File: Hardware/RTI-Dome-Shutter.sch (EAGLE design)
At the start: 42 parts, among them IC1 24AA128ST, IC5 74LVC245, IC6 74ABT245

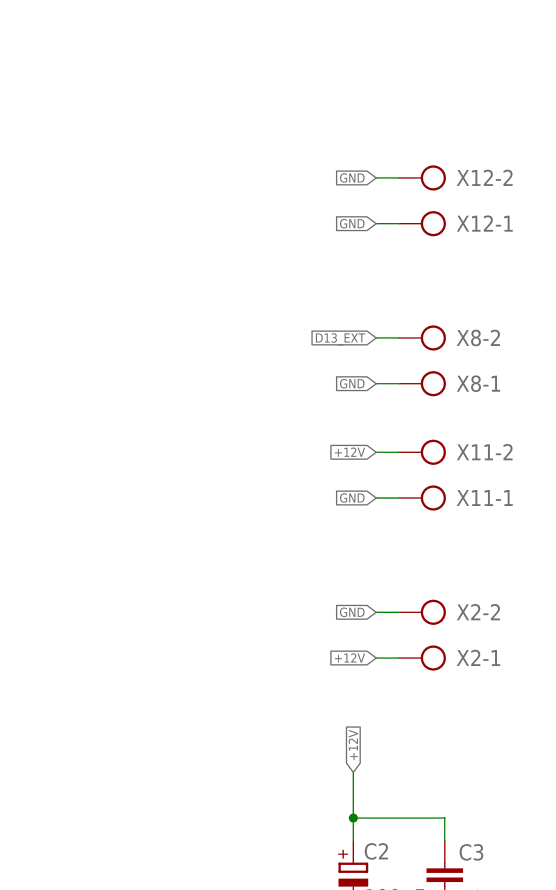
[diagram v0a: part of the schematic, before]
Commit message: Added powerpole to shutter shield
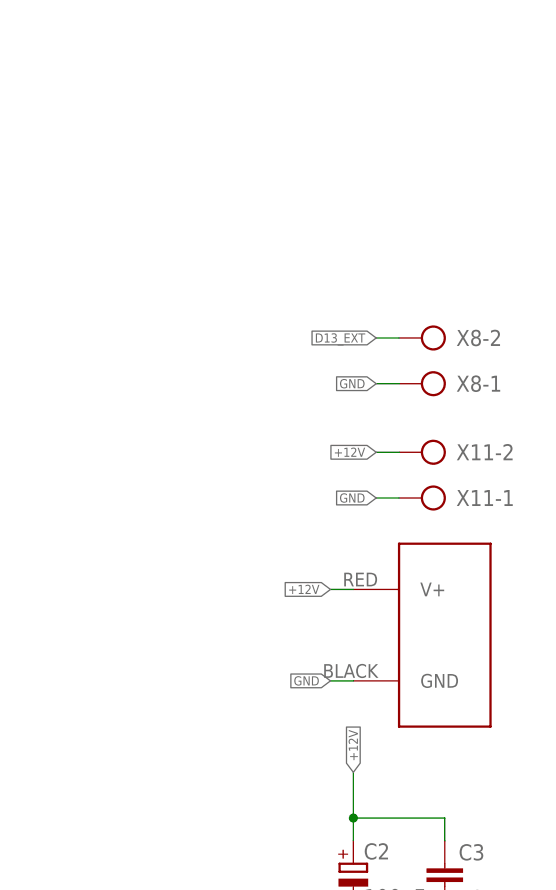
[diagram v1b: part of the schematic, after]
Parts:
- removed X12, X2: (no value), con-ptr500:AK500/2
- added J1: POWERPOLE_POWER45A, powerpoles:POWERPOLE_POWER45A
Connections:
- net +12V: now also J1.V+; no longer X2-1.KL
- net GND: now also J1.GND; no longer X12-1.KL, X12-2.KL, X2-2.KL
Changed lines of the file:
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@@
 </classes>
 <parts>
-<part name="X2" library="con-ptr500" deviceset="AK500/2" device=""/>
 <part name="X4" library="con-ptr500" deviceset="AK500/3" device=""/>
 <part name="X1" library="con-ptr500" deviceset="AK500/2" device=""/>
@@
 <part name="R3" library="rti" deviceset="R-EU" device="'0805'" value="1K"/>
 <part name="C5" library="rti" deviceset="C-EU" device="'0805'" value="100nF"/>
-<part name="X12" library="con-ptr500" deviceset="AK500/2" device=""/>
 <part name="GND12" library="supply1" deviceset="GND" device=""/>
 <part name="P+1" library="supply1" deviceset="VCC" device=""/>
@@
 <part name="GND7" library="supply1" deviceset="GND" device=""/>
 <part name="R22" library="rti" deviceset="R-EU" device="'0805'" value="4.7K"/>
+<part name="J1" library="powerpoles" deviceset="POWERPOLE_POWER" device="45A"/>
 </parts>
 <sheets>
@@
 </plain>
 <instances>
-<instance part="X2" gate="-1" x="378.46" y="81.28" rot="R180"/>
-<instance part="X2" gate="-2" x="378.46" y="86.36" rot="R180"/>
 <instance part="X4" gate="-1" x="378.46" y="218.44" rot="R180"/>
 <instance part="X4" gate="-2" x="378.46" y="223.52" rot="R180"/>
@@
 <instance part="R3" gate="G$1" x="40.64" y="248.92" rot="R90"/>
 <instance part="C5" gate="G$1" x="114.3" y="180.34"/>
-<instance part="X12" gate="-1" x="378.46" y="129.54" rot="R180"/>
-<instance part="X12" gate="-2" x="378.46" y="134.62" rot="R180"/>
 <instance part="GND12" gate="1" x="205.74" y="165.1"/>
 <instance part="P+1" gate="VCC" x="205.74" y="195.58"/>
@@
 <instance part="GND7" gate="1" x="187.96" y="226.06"/>
 <instance part="R22" gate="G$1" x="147.32" y="180.34" rot="R270"/>
+<instance part="J1" gate="G$1" x="378.46" y="83.82"/>
 </instances>
 <busses>
@@
 </segment>
 <segment>
-<pinref part="X2" gate="-2" pin="KL"/>
-<wire x1="370.84" y1="86.36" x2="373.38" y2="86.36" width="0.1524" layer="91"/>
-<label x="370.84" y="86.36" size="1.016" layer="95" rot="R180" xref="yes"/>
+<wire x1="365.76" y1="78.74" x2="368.3" y2="78.74" width="0.1524" layer="91"/>
+<label x="365.76" y="78.74" size="1.016" layer="95" rot="R180" xref="yes"/>
+<pinref part="J1" gate="G$1" pin="GND"/>
 </segment>
 <segment>
@@
 </segment>
 <segment>
-<pinref part="X12" gate="-1" pin="KL"/>
-<wire x1="370.84" y1="129.54" x2="373.38" y2="129.54" width="0.1524" layer="91"/>
-<label x="370.84" y="129.54" size="1.016" layer="95" rot="R180" xref="yes"/>
-</segment>
-<segment>
 <wire x1="116.84" y1="243.84" x2="119.38" y2="243.84" width="0.1524" layer="91"/>
 <label x="116.84" y="243.84" size="0.8128" layer="95" rot="R180" xref="yes"/>
@@
 <label x="187.96" y="238.76" size="0.8128" layer="95" rot="R180" xref="yes"/>
 <pinref part="IC6" gate="G$1" pin="A7"/>
-</segment>
-<segment>
-<pinref part="X12" gate="-2" pin="KL"/>
-<wire x1="370.84" y1="134.62" x2="373.38" y2="134.62" width="0.1524" layer="91"/>
-<label x="370.84" y="134.62" size="1.016" layer="95" rot="R180" xref="yes"/>
 </segment>
 <segment>
@@
 </segment>
 <segment>
-<pinref part="X2" gate="-1" pin="KL"/>
-<wire x1="370.84" y1="81.28" x2="373.38" y2="81.28" width="0.1524" layer="91"/>
-<label x="370.84" y="81.28" size="1.016" layer="95" rot="R180" xref="yes"/>
-</segment>
-<segment>
+<wire x1="365.76" y1="88.9" x2="368.3" y2="88.9" width="0.1524" layer="91"/>
+<label x="365.76" y="88.9" size="1.016" layer="95" rot="R180" xref="yes"/>
+<pinref part="J1" gate="G$1" pin="V+"/>
+</segment>
+<segment>

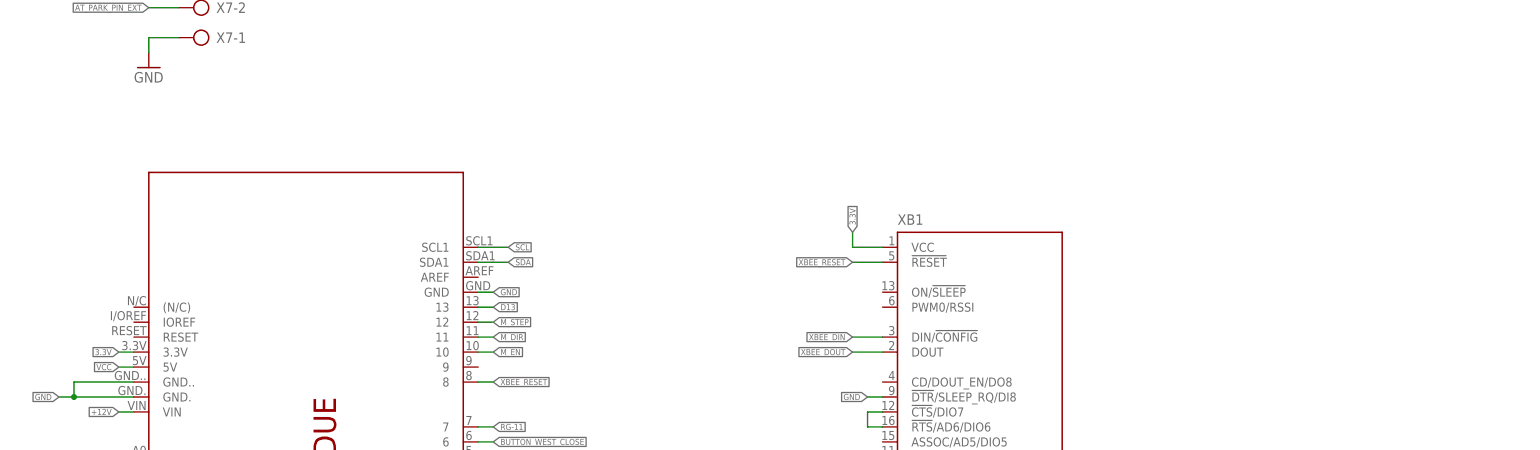
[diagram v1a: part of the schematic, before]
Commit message: Adding MCP120 for power on reset.
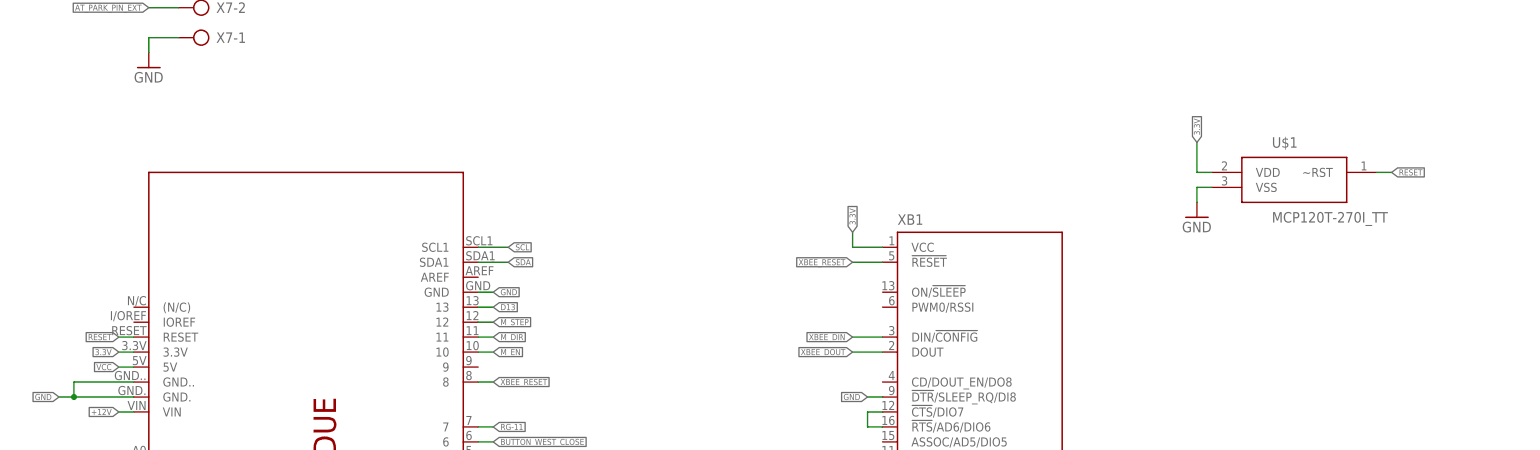
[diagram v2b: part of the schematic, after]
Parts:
- added U$1: MCP120T-270I_TT, MCP120T-270I_TT:MCP120T-270I_TT
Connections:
- new net RESET: PCB1.RESET, U$1.~RST
- net 3.3V: now also U$1.VDD
- net GND: now also U$1.VSS
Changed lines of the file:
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@@
 <part name="R22" library="rti" deviceset="R-EU" device="'0805'" value="4.7K"/>
 <part name="J1" library="powerpoles" deviceset="POWERPOLE_POWER" device="45A"/>
+<part name="U$1" library="MCP120T-270I_TT" deviceset="MCP120T-270I_TT" device=""/>
+<part name="GND9" library="supply1" deviceset="GND" device=""/>
 </parts>
 <sheets>
@@
 <instance part="R22" gate="G$1" x="147.32" y="180.34" rot="R270"/>
 <instance part="J1" gate="G$1" x="378.46" y="83.82"/>
+<instance part="U$1" gate="G$1" x="218.44" y="93.98"/>
+<instance part="GND9" gate="1" x="203.2" y="86.36"/>
 </instances>
 <busses>
@@
 <pinref part="GND7" gate="1" pin="GND"/>
 </segment>
+<segment>
+<pinref part="U$1" gate="G$1" pin="VSS"/>
+<wire x1="205.74" y1="91.44" x2="203.2" y2="91.44" width="0.1524" layer="91"/>
+<wire x1="203.2" y1="91.44" x2="203.2" y2="88.9" width="0.1524" layer="91"/>
+<pinref part="GND9" gate="1" pin="GND"/>
+</segment>
 </net>
 <net name="+12V" class="1">
@@
 <wire x1="116.84" y1="231.14" x2="119.38" y2="231.14" width="0.1524" layer="91"/>
 <label x="116.84" y="231.14" size="1.016" layer="95" rot="R180" xref="yes"/>
+</segment>
+<segment>
+<pinref part="U$1" gate="G$1" pin="VDD"/>
+<wire x1="205.74" y1="93.98" x2="203.2" y2="93.98" width="0.1524" layer="91"/>
+<wire x1="203.2" y1="93.98" x2="203.2" y2="99.06" width="0.1524" layer="91"/>
+<label x="203.2" y="99.06" size="1.016" layer="95" rot="R90" xref="yes"/>
 </segment>
 </net>
@@
 </segment>
 </net>
+<net name="RESET" class="0">
+<segment>
+<pinref part="PCB1" gate="G$1" pin="RESET"/>
+<wire x1="20.32" y1="66.04" x2="22.86" y2="66.04" width="0.1524" layer="91"/>
+<label x="20.32" y="66.04" size="1.016" layer="95" rot="R180" xref="yes"/>
+</segment>
+<segment>
+<pinref part="U$1" gate="G$1" pin="~RST"/>
+<wire x1="236.22" y1="93.98" x2="233.68" y2="93.98" width="0.1524" layer="91"/>
+<label x="236.22" y="93.98" size="1.016" layer="95" xref="yes"/>
+</segment>
+</net>

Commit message: Fix some componenent manufacturer reference
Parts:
- IC6: device rti:74LVC245 -> rti:74ABT245
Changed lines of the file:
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@@
 <part name="X6" library="con-ptr500" deviceset="AK500/6" device=""/>
 <part name="IC5" library="rti" deviceset="74*245" device="" technology="LVC"/>
-<part name="IC6" library="rti" deviceset="74*245" device="" technology="LVC" value="74ABT245"/>
+<part name="IC6" library="rti" deviceset="74*245" device="" technology="ABT" value="74ABT245"/>
 <part name="GND7" library="supply1" deviceset="GND" device=""/>
 <part name="R22" library="rti" deviceset="R-EU" device="'0805'" value="4.7K"/>

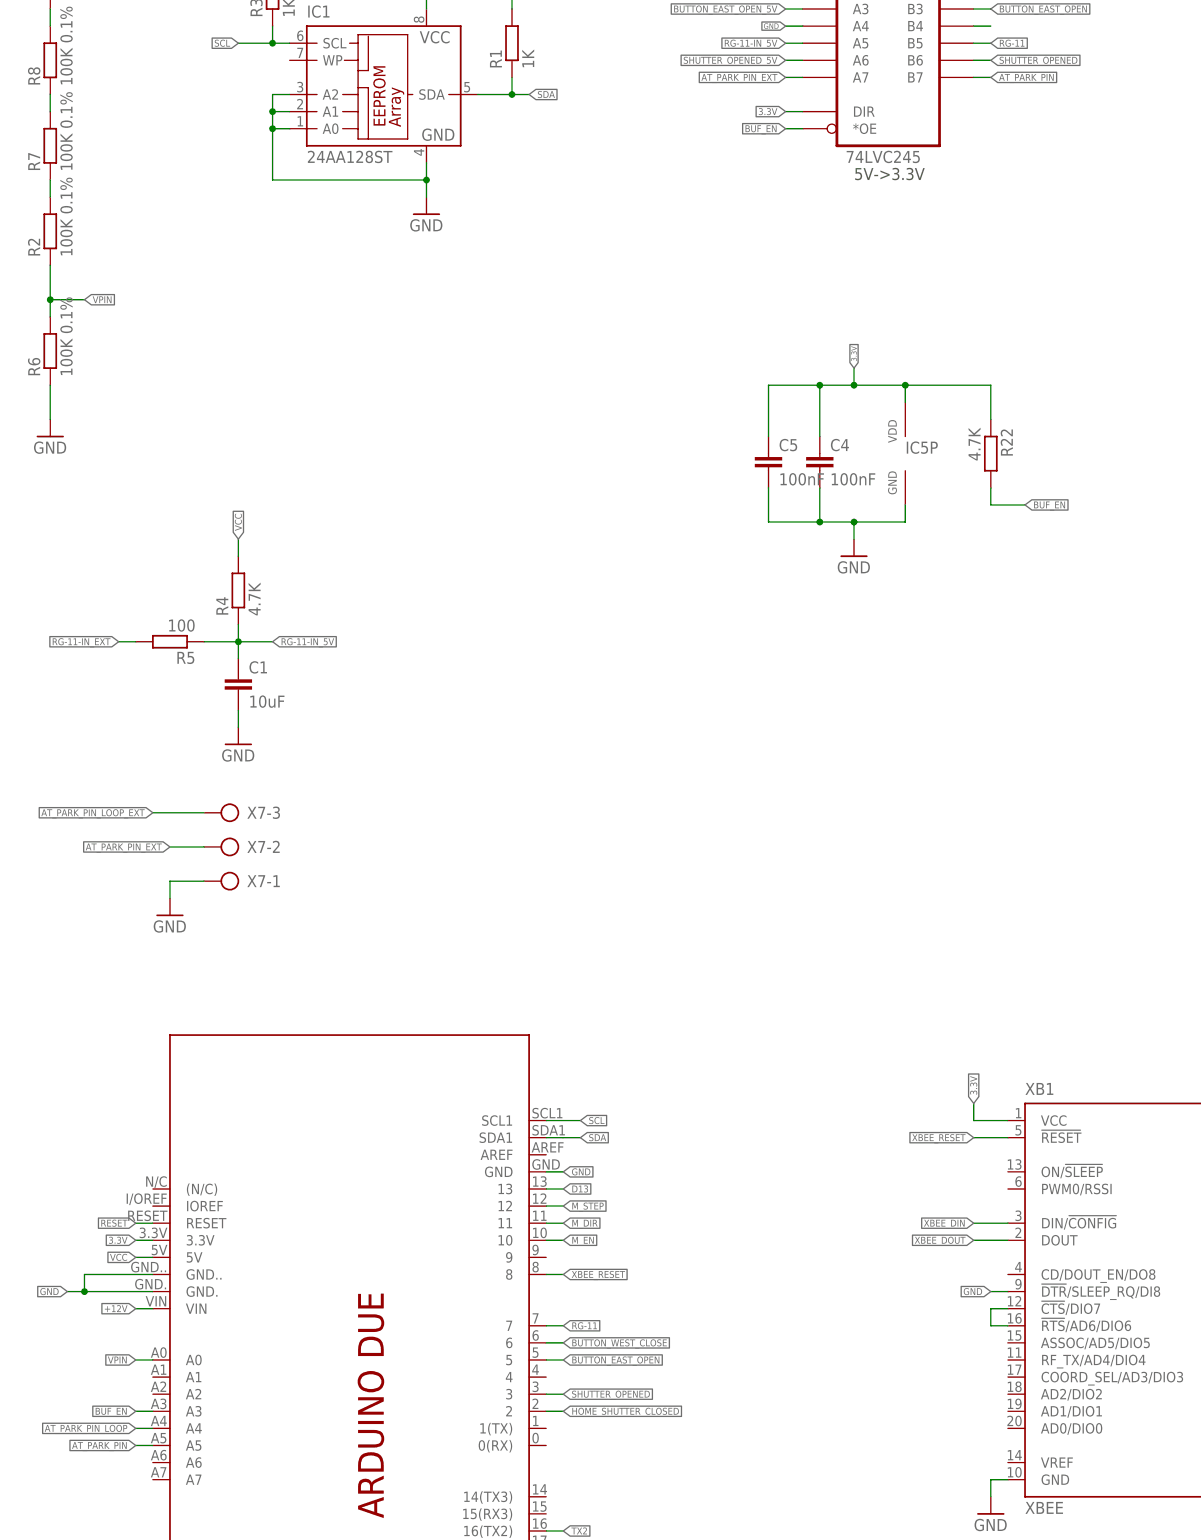
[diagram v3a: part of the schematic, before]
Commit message: Added FTDI reset as it wasn't doing a proper reset on power up. Finished IP config in the plugin.
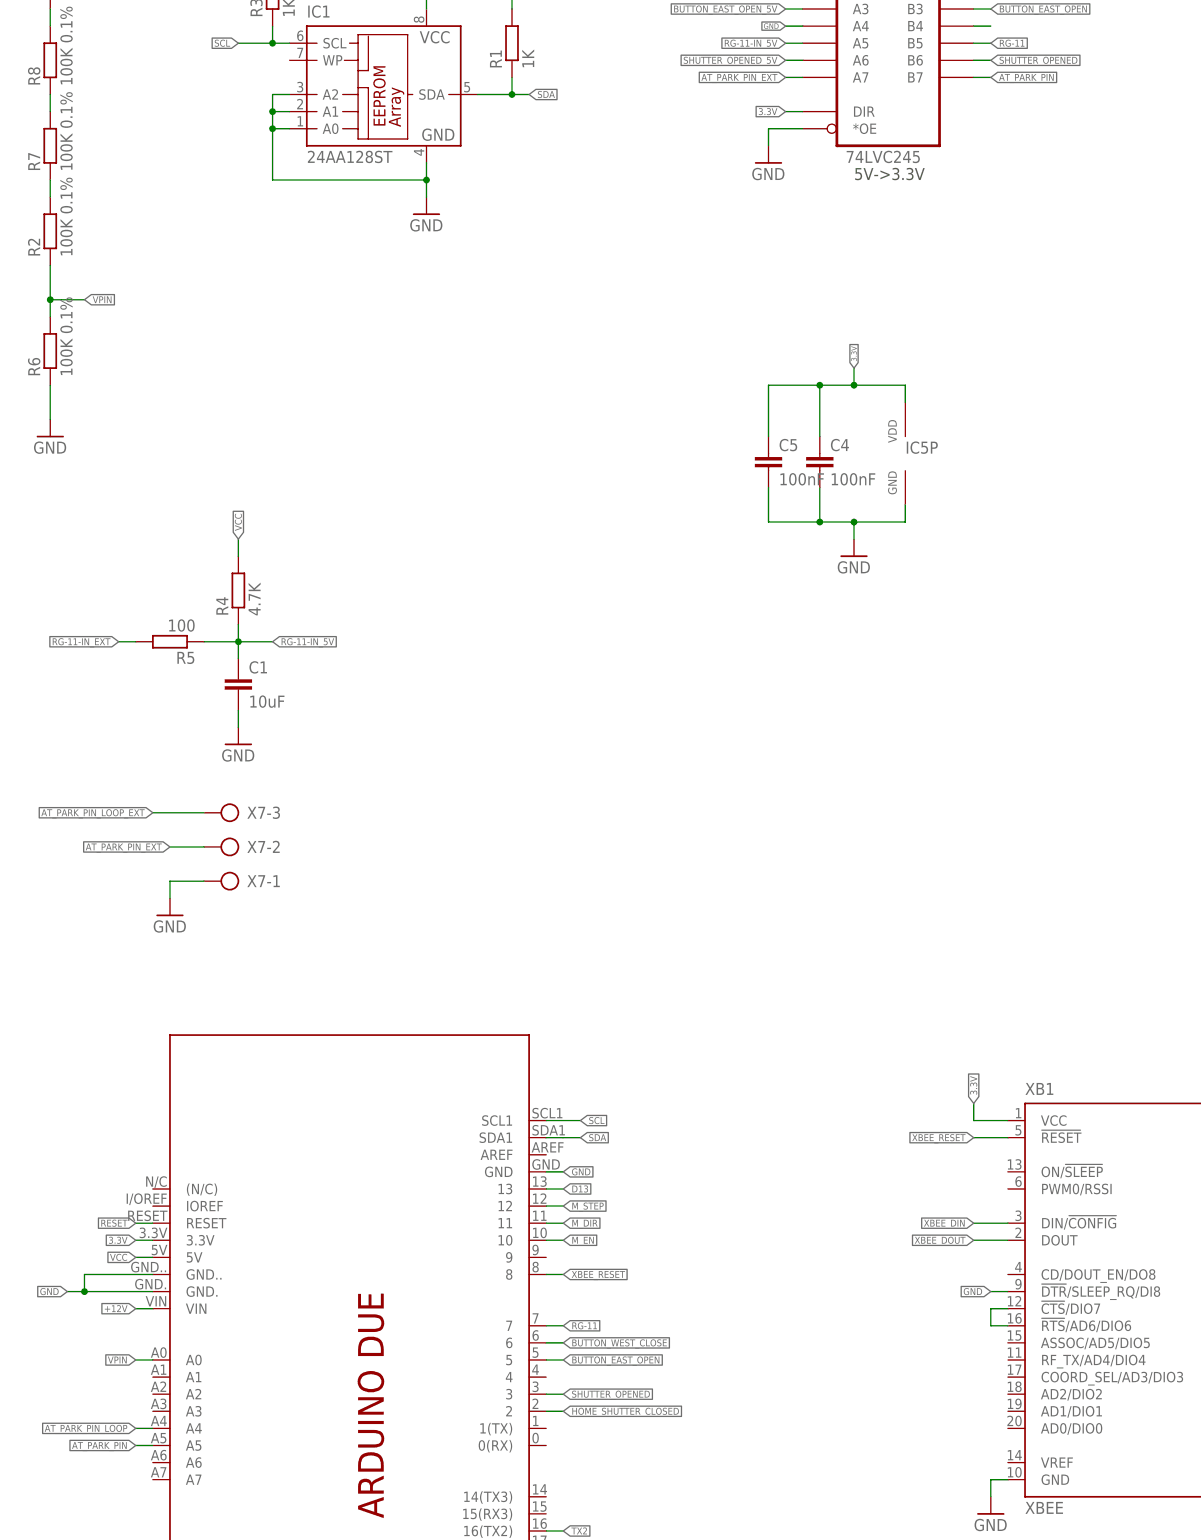
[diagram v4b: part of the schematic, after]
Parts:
- removed R22: 4.7K, rti:R-EU'0805'
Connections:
- removed net BUF_EN: IC5G$1.*OE, PCB1.A3, R22.2
- net 3.3V: no longer R22.1
- net GND: now also IC5G$1.*OE
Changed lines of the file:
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@@
 <part name="IC6" library="rti" deviceset="74*245" device="" technology="ABT" value="74ABT245"/>
 <part name="GND7" library="supply1" deviceset="GND" device=""/>
-<part name="R22" library="rti" deviceset="R-EU" device="'0805'" value="4.7K"/>
 <part name="J1" library="powerpoles" deviceset="POWERPOLE_POWER" device="45A"/>
 <part name="U$1" library="MCP120T-270I_TT" deviceset="MCP120T-270I_TT" device=""/>
 <part name="GND9" library="supply1" deviceset="GND" device=""/>
+<part name="GND10" library="supply1" deviceset="GND" device=""/>
 </parts>
 <sheets>
@@
 <instance part="IC6" gate="P" x="203.2" y="180.34" rot="R270"/>
 <instance part="GND7" gate="1" x="187.96" y="226.06"/>
-<instance part="R22" gate="G$1" x="147.32" y="180.34" rot="R270"/>
 <instance part="J1" gate="G$1" x="378.46" y="83.82"/>
 <instance part="U$1" gate="G$1" x="218.44" y="93.98"/>
 <instance part="GND9" gate="1" x="203.2" y="86.36"/>
+<instance part="GND10" gate="1" x="114.3" y="223.52"/>
 </instances>
 <busses>
@@
 <pinref part="GND9" gate="1" pin="GND"/>
 </segment>
+<segment>
+<pinref part="IC5" gate="G$1" pin="*OE"/>
+<wire x1="119.38" y1="228.6" x2="114.3" y2="228.6" width="0.1524" layer="91"/>
+<wire x1="114.3" y1="228.6" x2="114.3" y2="226.06" width="0.1524" layer="91"/>
+<pinref part="GND10" gate="1" pin="GND"/>
+</segment>
 </net>
 <net name="+12V" class="1">
@@
 <junction x="121.92" y="190.5"/>
 <pinref part="IC5" gate="P" pin="VDD"/>
-<pinref part="R22" gate="G$1" pin="1"/>
-<wire x1="134.62" y1="190.5" x2="147.32" y2="190.5" width="0.1524" layer="91"/>
-<wire x1="147.32" y1="190.5" x2="147.32" y2="185.42" width="0.1524" layer="91"/>
-<junction x="134.62" y="190.5"/>
 </segment>
 <segment>
@@
 </segment>
 </net>
-<net name="BUF_EN" class="0">
-<segment>
-<pinref part="IC5" gate="G$1" pin="*OE"/>
-<wire x1="116.84" y1="228.6" x2="119.38" y2="228.6" width="0.1524" layer="91"/>
-<label x="116.84" y="228.6" size="1.016" layer="95" rot="R180" xref="yes"/>
-</segment>
-<segment>
-<pinref part="R22" gate="G$1" pin="2"/>
-<wire x1="152.4" y1="172.72" x2="147.32" y2="172.72" width="0.1524" layer="91"/>
-<wire x1="147.32" y1="172.72" x2="147.32" y2="175.26" width="0.1524" layer="91"/>
-<label x="152.4" y="172.72" size="1.016" layer="95" xref="yes"/>
-</segment>
-<segment>
-<pinref part="PCB1" gate="G$1" pin="A3"/>
-<wire x1="20.32" y1="38.1" x2="22.86" y2="38.1" width="0.1524" layer="91"/>
-<label x="20.32" y="38.1" size="1.016" layer="95" rot="R180" xref="yes"/>
-</segment>
-</net>

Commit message: Made some changes to the shutter controller to be able to control axtra linear actuator via external relay board.
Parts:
- removed R20, R21: 4.7K, rti:R-EU'0805'
- added C7: 10uF, rti:C-EU'0805'
- added R11: 100, rti:R-EU'0805'
- added R9: 4.7K, rti:R-EU'0805'
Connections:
- net AT_PARK_PIN_LOOP renamed A4_OUT
- net AT_PARK_PIN_LOOP_EXT renamed A4_OUT_5V
- net D13 renamed D13_IN
- net RG-11 renamed D7_IN
- net RG-11-IN_5V renamed D7-IN_5V
- net RG-11-IN_EXT renamed D7-IN_EXT
- removed net AT_PARK_PIN: IC5G$1.B7, PCB1.A5
- removed net AT_PARK_PIN_EXT: IC5G$1.A7, R20.1, X7-2.KL
- new net D13_EXT_5V: C7.1, IC5G$1.A0, R11.1, R9.1
- new net D9_OUT: IC6G$1.A4, PCB1.9
- new net D9_OUT_5V: IC6G$1.B4, X7-2.KL
- net D13_EXT: now also R11.2; no longer IC5G$1.A0, R21.2
- net GND: now also C7.2; no longer IC6G$1.A4
- net VCC: now also R9.2; no longer R20.2, R21.1
